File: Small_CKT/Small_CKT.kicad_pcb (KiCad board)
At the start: 2 copper layers, 38.2 x 38.2 mm, 5 parts, among them SW1 SW_Push

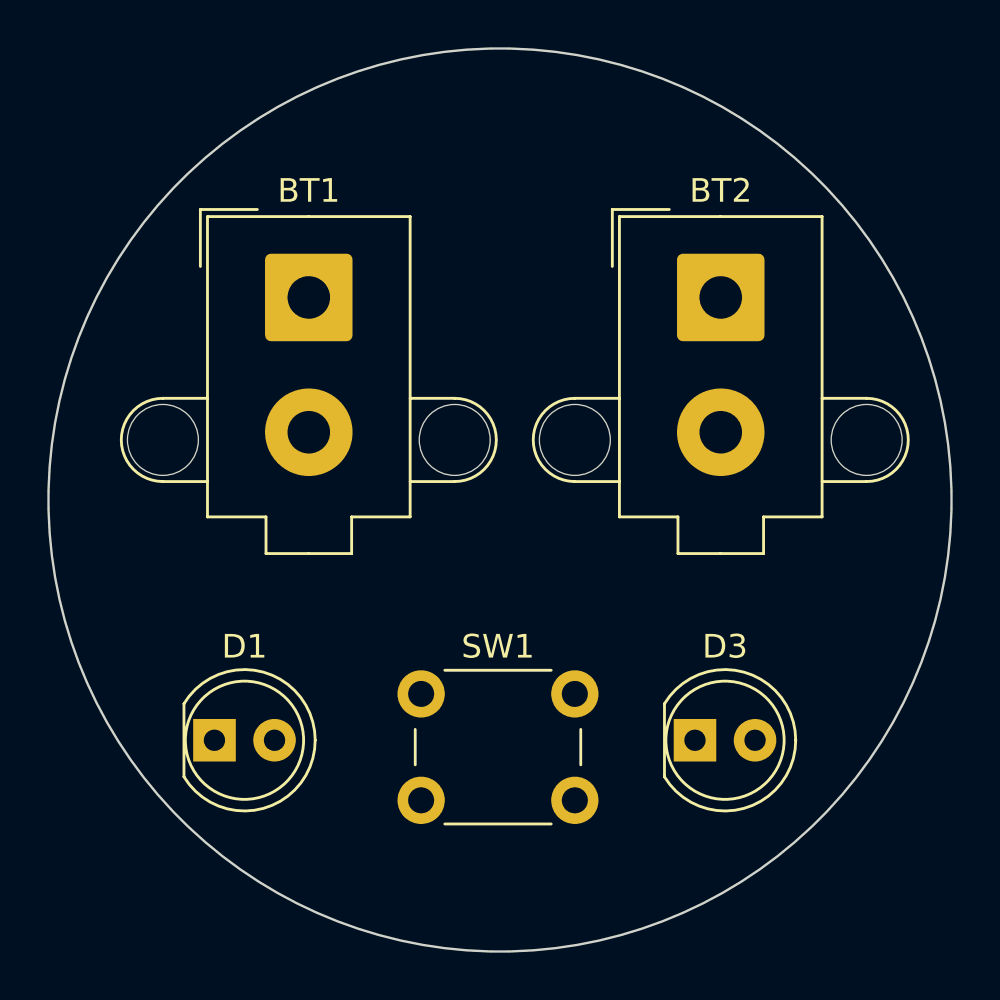
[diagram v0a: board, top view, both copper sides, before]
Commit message: Added traces in layout
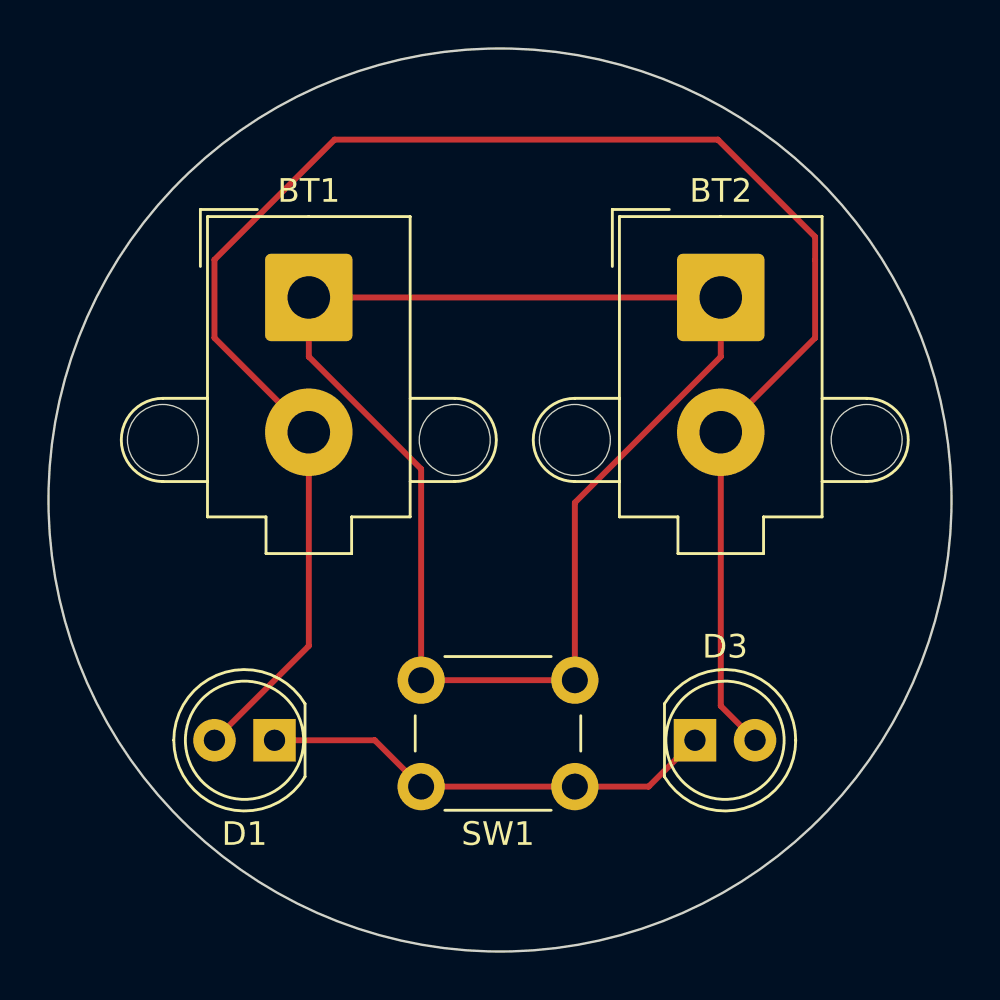
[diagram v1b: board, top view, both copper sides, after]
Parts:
- moved SW1 7.59 mm to (137.2, 111.2), turned to 180 degrees
- moved D1 2.54 mm to (124.5, 109.2), turned to 180 degrees
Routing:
- net GND: track 0.00 -> 76.4 mm
- net Net-(BT1-+): track 0.00 -> 60.8 mm
- net Net-(D1-K): track 0.00 -> 19.4 mm
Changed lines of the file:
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@@
   (net 3 "Net-(D1-K)")
   (footprint "LED_THT:LED_D5.0mm_Clear" (layer "F.Cu")
-    (at 121.92 109.22)
+    (at 124.46 109.22 180)
     (descr "LED, diameter 5.0mm, 2 pins, http://cdn-reichelt.de/documents/datenblatt/A500/LL-504BC2E-009.pdf")
     (tags "LED diameter 5.0mm 2 pins")
@@
     (fp_circle (center 1.27 0) (end 3.77 0)
       (stroke (width 0.1) (type solid)) (fill none) (layer "F.Fab"))
-    (pad "1" thru_hole rect (at 0 0) (size 1.8 1.8) (drill 0.9) (layers "*.Cu" "*.Mask")
+    (pad "1" thru_hole rect (at 0 0 180) (size 1.8 1.8) (drill 0.9) (layers "*.Cu" "*.Mask")
       (net 3 "Net-(D1-K)") (pinfunction "K") (pintype "passive"))
-    (pad "2" thru_hole circle (at 2.54 0) (size 1.8 1.8) (drill 0.9) (layers "*.Cu" "*.Mask")
+    (pad "2" thru_hole circle (at 2.54 0 180) (size 1.8 1.8) (drill 0.9) (layers "*.Cu" "*.Mask")
       (net 2 "GND") (pinfunction "A") (pintype "passive"))
     (model "${KICAD6_3DMODEL_DIR}/LED_THT.3dshapes/LED_D5.0mm_Clear.wrl"
@@
   )
   (footprint "Button_Switch_THT:SW_PUSH_6mm" (layer "F.Cu")
-    (at 130.66 107.26)
+    (at 137.16 111.18 180)
     (descr "https://www.omron.com/ecb/products/pdf/en-b3f.pdf")
     (tags "tact sw push 6mm")
@@
     (fp_circle (center 3.25 2.25) (end 1.25 2.5)
       (stroke (width 0.1) (type solid)) (fill none) (layer "F.Fab"))
-    (pad "1" thru_hole circle (at 0 0 90) (size 2 2) (drill 1.1) (layers "*.Cu" "*.Mask")
+    (pad "1" thru_hole circle (at 0 0 270) (size 2 2) (drill 1.1) (layers "*.Cu" "*.Mask")
       (net 3 "Net-(D1-K)") (pinfunction "1") (pintype "passive"))
-    (pad "1" thru_hole circle (at 6.5 0 90) (size 2 2) (drill 1.1) (layers "*.Cu" "*.Mask")
+    (pad "1" thru_hole circle (at 6.5 0 270) (size 2 2) (drill 1.1) (layers "*.Cu" "*.Mask")
       (net 3 "Net-(D1-K)") (pinfunction "1") (pintype "passive"))
-    (pad "2" thru_hole circle (at 0 4.5 90) (size 2 2) (drill 1.1) (layers "*.Cu" "*.Mask")
+    (pad "2" thru_hole circle (at 0 4.5 270) (size 2 2) (drill 1.1) (layers "*.Cu" "*.Mask")
       (net 1 "Net-(BT1-+)") (pinfunction "2") (pintype "passive"))
-    (pad "2" thru_hole circle (at 6.5 4.5 90) (size 2 2) (drill 1.1) (layers "*.Cu" "*.Mask")
+    (pad "2" thru_hole circle (at 6.5 4.5 270) (size 2 2) (drill 1.1) (layers "*.Cu" "*.Mask")
       (net 1 "Net-(BT1-+)") (pinfunction "2") (pintype "passive"))
     (model "${KICAD6_3DMODEL_DIR}/Button_Switch_THT.3dshapes/SW_PUSH_6mm.wrl"
@@
   (gr_circle (center 133.994624 99.06) (end 152.4 104.14)
     (stroke (width 0.1) (type default)) (fill none) (layer "Edge.Cuts"))
+  (segment (start 125.91 93.00165) (end 130.66 97.75165) (width 0.25) (layer "F.Cu") (net 1))
+  (segment (start 143.33 90.495) (end 143.33 93.00165) (width 0.25) (layer "F.Cu") (net 1))
+  (segment (start 137.16 106.68) (end 130.66 106.68) (width 0.25) (layer "F.Cu") (net 1))
+  (segment (start 125.91 90.495) (end 125.91 93.00165) (width 0.25) (layer "F.Cu") (net 1))
+  (segment (start 143.33 93.00165) (end 137.16 99.17165) (width 0.25) (layer "F.Cu") (net 1))
+  (segment (start 125.91 90.495) (end 143.33 90.495) (width 0.25) (layer "F.Cu") (net 1))
+  (segment (start 130.66 97.75165) (end 130.66 106.68) (width 0.25) (layer "F.Cu") (net 1))
+  (segment (start 137.16 99.17165) (end 137.16 106.68) (width 0.25) (layer "F.Cu") (net 1))
+  (segment (start 143.208172 83.82) (end 127 83.82) (width 0.25) (layer "F.Cu") (net 2))
+  (segment (start 121.92 109.22) (end 125.91 105.23) (width 0.25) (layer "F.Cu") (net 2))
+  (segment (start 143.33 96.195) (end 143.33 107.77) (width 0.25) (layer "F.Cu") (net 2))
+  (segment (start 147.32 88.9) (end 147.32 87.931828) (width 0.25) (layer "F.Cu") (net 2))
+  (segment (start 125.91 105.23) (end 125.91 96.195) (width 0.25) (layer "F.Cu") (net 2))
+  (segment (start 127 83.82) (end 121.92 88.9) (width 0.25) (layer "F.Cu") (net 2))
+  (segment (start 121.92 88.9) (end 121.92 92.205) (width 0.25) (layer "F.Cu") (net 2))
+  (segment (start 121.92 92.205) (end 125.91 96.195) (width 0.25) (layer "F.Cu") (net 2))
+  (segment (start 147.32 87.931828) (end 143.208172 83.82) (width 0.25) (layer "F.Cu") (net 2))
+  (segment (start 143.33 96.195) (end 147.32 92.205) (width 0.25) (layer "F.Cu") (net 2))
+  (segment (start 143.33 107.77) (end 144.78 109.22) (width 0.25) (layer "F.Cu") (net 2))
+  (segment (start 147.32 92.205) (end 147.32 88.9) (width 0.25) (layer "F.Cu") (net 2))
+  (segment (start 130.66 111.18) (end 137.16 111.18) (width 0.25) (layer "F.Cu") (net 3))
+  (segment (start 124.46 109.22) (end 128.7 109.22) (width 0.25) (layer "F.Cu") (net 3))
+  (segment (start 128.7 109.22) (end 130.66 111.18) (width 0.25) (layer "F.Cu") (net 3))
+  (segment (start 137.16 111.18) (end 140.28 111.18) (width 0.25) (layer "F.Cu") (net 3))
+  (segment (start 140.28 111.18) (end 142.24 109.22) (width 0.25) (layer "F.Cu") (net 3))
 )
